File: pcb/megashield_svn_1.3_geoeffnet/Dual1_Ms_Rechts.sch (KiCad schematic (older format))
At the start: 7 parts, among them P18 Right

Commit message: Platine V1.3
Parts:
- renumbered BY1 to DBY1, BY2 to DBY2, BY3 to DBY3, BY4 to DBY4
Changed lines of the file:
@@
 LIBS:power
 LIBS:ardumower mega shield svn-cache
+LIBS:conn
 EELAYER 25 0
 EELAYER END
@@
 MotorRechtsB
 $Comp
-L +24V #PWR0137
+L +24V #PWR0139
 U 1 1 554BE90F
 P 4895 3310
-F 0 "#PWR0137" H 4895 3160 60  0001 C CNN
+F 0 "#PWR0139" H 4895 3160 60  0001 C CNN
 F 1 "+24V" H 4895 3450 60  0000 C CNN
 F 2 "" H 4895 3310 60  0000 C CNN
@@
 $EndComp
 $Comp
-L GND #PWR0138
+L GND #PWR0140
 U 1 1 554BE911
 P 4895 4445
-F 0 "#PWR0138" H 4895 4195 60  0001 C CNN
+F 0 "#PWR0140" H 4895 4195 60  0001 C CNN
 F 1 "GND" H 4895 4295 60  0000 C CNN
 F 2 "" H 4895 4445 60  0000 C CNN
@@
 $EndComp
 $Comp
-L DIODE BY3
+L DIODE DBY3
 U 1 1 554BE913
 P 4895 3580
-F 0 "BY3" H 4895 3680 40  0000 C CNN
+F 0 "DBY3" H 4895 3680 40  0000 C CNN
 F 1 "BY 500/1000" H 4895 3480 40  0000 C CNN
 F 2 "ACS712:Diode_liegend_BY500_1000_RM15" H 4895 3580 60  0001 C CNN
@@
 $EndComp
 $Comp
-L DIODE BY4
+L DIODE DBY4
 U 1 1 554BE915
 P 4895 4140
-F 0 "BY4" H 4895 4240 40  0000 C CNN
+F 0 "DBY4" H 4895 4240 40  0000 C CNN
 F 1 "BY 500/1000" H 4895 4040 40  0000 C CNN
 F 2 "ACS712:Diode_liegend_BY500_1000_RM15" H 4895 4140 60  0001 C CNN
@@
 Connection ~ 4895 3870
 $Comp
-L +24V #PWR0139
+L +24V #PWR0141
 U 1 1 554BE918
 P 3170 3310
-F 0 "#PWR0139" H 3170 3160 60  0001 C CNN
+F 0 "#PWR0141" H 3170 3160 60  0001 C CNN
 F 1 "+24V" H 3170 3450 60  0000 C CNN
 F 2 "" H 3170 3310 60  0000 C CNN
@@
 $EndComp
 $Comp
-L GND #PWR0140
+L GND #PWR0142
 U 1 1 554BE91A
 P 3170 4445
-F 0 "#PWR0140" H 3170 4195 60  0001 C CNN
+F 0 "#PWR0142" H 3170 4195 60  0001 C CNN
 F 1 "GND" H 3170 4295 60  0000 C CNN
 F 2 "" H 3170 4445 60  0000 C CNN
@@
 $EndComp
 $Comp
-L DIODE BY1
+L DIODE DBY1
 U 1 1 554BE91C
 P 3170 3580
-F 0 "BY1" H 3170 3680 40  0000 C CNN
+F 0 "DBY1" H 3170 3680 40  0000 C CNN
 F 1 "BY 500/1000" H 3170 3480 40  0000 C CNN
 F 2 "ACS712:Diode_liegend_BY500_1000_RM15" H 3170 3580 60  0001 C CNN
@@
 $EndComp
 $Comp
-L DIODE BY2
+L DIODE DBY2
 U 1 1 554BE91E
 P 3170 4140
-F 0 "BY2" H 3170 4240 40  0000 C CNN
+F 0 "DBY2" H 3170 4240 40  0000 C CNN
 F 1 "BY 500/1000" H 3170 4040 40  0000 C CNN
 F 2 "ACS712:Diode_liegend_BY500_1000_RM15" H 3170 4140 60  0001 C CNN

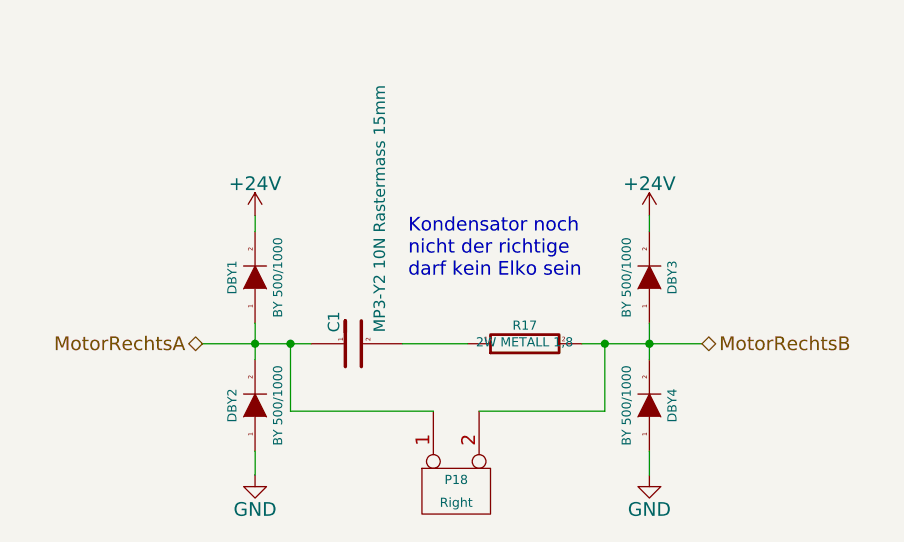
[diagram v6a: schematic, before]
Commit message: Platine V1.3
Einzelne Bauteile auf SMD angepasst
Belegung Anschlussstecker geändert +5V und GND
Anschlussstecker auf KK Stecker umgeändert
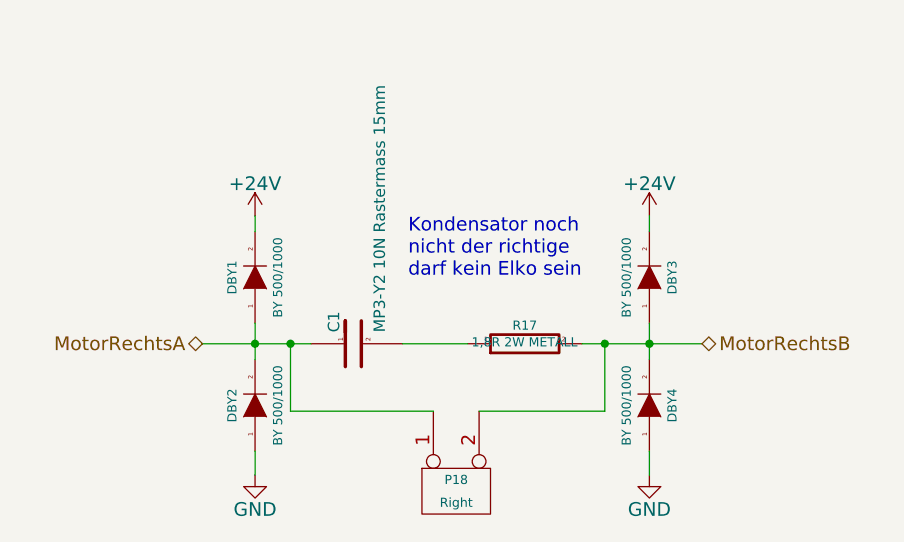
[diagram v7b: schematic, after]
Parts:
- DBY1, DBY2, DBY3, DBY4: footprint ACS712:Diode_liegend_BY500_1000_RM15 -> Diodes_ThroughHole:Diode_DO-201AD_Horizontal_RM15; Bauform (none) -> DO-201; Bestelllink (none) -> https://www.reichelt.de/BY-500-1000/3/index.html?&ACTION=3&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
- R17: value 2W METALL 1,8 -> 1,8R 2W METALL; footprint Resistors_ThroughHole:Resistor_Horizontal_RM20mm -> Resistors_SMD:R_2512
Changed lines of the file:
@@
 $Descr A4 11693 8268
 encoding utf-8
-Sheet 13 27
+Sheet 13 25
 Title "Ardumower Shield - Motortreiber 1 - Rechts"
 Date ""
@@
 MotorRechtsB
 $Comp
-L +24V #PWR0143
+L +24V #PWR0153
 U 1 1 554BE90F
 P 4895 3310
-F 0 "#PWR0143" H 4895 3160 60  0001 C CNN
+F 0 "#PWR0153" H 4895 3160 60  0001 C CNN
 F 1 "+24V" H 4895 3450 60  0000 C CNN
 F 2 "" H 4895 3310 60  0000 C CNN
@@
 $EndComp
 $Comp
-L GND #PWR0144
+L GND #PWR0154
 U 1 1 554BE911
 P 4895 4445
-F 0 "#PWR0144" H 4895 4195 60  0001 C CNN
+F 0 "#PWR0154" H 4895 4195 60  0001 C CNN
 F 1 "GND" H 4895 4295 60  0000 C CNN
 F 2 "" H 4895 4445 60  0000 C CNN
@@
 F 0 "DBY3" H 4895 3680 40  0000 C CNN
 F 1 "BY 500/1000" H 4895 3480 40  0000 C CNN
-F 2 "ACS712:Diode_liegend_BY500_1000_RM15" H 4895 3580 60  0001 C CNN
+F 2 "Diodes_ThroughHole:Diode_DO-201AD_Horizontal_RM15" H 4895 3580 60  0001 C CNN
 F 3 "https://www.reichelt.de/BY-500-1000/3/index.html?&ACTION=3&LA=446&ARTICLE=6337&artnr=BY+500%2F1000&SEARCH=BY+500%2F1000" H 4895 3580 60  0001 C CNN
-F 4 "R: BY 500/1000" H 4895 3580 60  0001 C CNN "Bestellnummer"
-F 5 "Fast-Recovery-Gleichr.-Diode, DO201, 1000V, 5A" H 4895 3580 60  0001 C CNN "Technische Daten"
+F 4 "Fast-Recovery-Gleichr.-Diode, DO201, 1000V, 5A" H 4895 3580 60  0001 C CNN "Technische Daten"
+F 5 "R: BY 500/1000" H 4895 3580 60  0001 C CNN "Bestellnummer"
+F 6 "DO-201" H 4895 3580 60  0001 C CNN "Bauform"
+F 7 "https://www.reichelt.de/BY-500-1000/3/index.html?&ACTION=3&LA=446&ARTICLE=6337&artnr=BY+500%2F1000&SEARCH=BY+500%2F1000" H 4895 3580 60  0001 C CNN "Bestelllink"
 	1    4895 3580
 	0    1    -1   0
@@
 F 0 "DBY4" H 4895 4240 40  0000 C CNN
 F 1 "BY 500/1000" H 4895 4040 40  0000 C CNN
-F 2 "ACS712:Diode_liegend_BY500_1000_RM15" H 4895 4140 60  0001 C CNN
+F 2 "Diodes_ThroughHole:Diode_DO-201AD_Horizontal_RM15" H 4895 4140 60  0001 C CNN
 F 3 "https://www.reichelt.de/BY-500-1000/3/index.html?&ACTION=3&LA=446&ARTICLE=6337&artnr=BY+500%2F1000&SEARCH=BY+500%2F1000" H 4895 4140 60  0001 C CNN
-F 4 "R: BY 500/1000" H 4895 4140 60  0001 C CNN "Bestellnummer"
-F 5 "Fast-Recovery-Gleichr.-Diode, DO201, 1000V, 5A" H 4895 4140 60  0001 C CNN "Technische Daten"
+F 4 "Fast-Recovery-Gleichr.-Diode, DO201, 1000V, 5A" H 4895 4140 60  0001 C CNN "Technische Daten"
+F 5 "R: BY 500/1000" H 4895 4140 60  0001 C CNN "Bestellnummer"
+F 6 "DO-201" H 4895 4140 60  0001 C CNN "Bauform"
+F 7 "https://www.reichelt.de/BY-500-1000/3/index.html?&ACTION=3&LA=446&ARTICLE=6337&artnr=BY+500%2F1000&SEARCH=BY+500%2F1000" H 4895 4140 60  0001 C CNN "Bestelllink"
 	1    4895 4140
 	0    1    -1   0
@@
 Connection ~ 4895 3870
 $Comp
-L +24V #PWR0145
+L +24V #PWR0155
 U 1 1 554BE918
 P 3170 3310
-F 0 "#PWR0145" H 3170 3160 60  0001 C CNN
+F 0 "#PWR0155" H 3170 3160 60  0001 C CNN
 F 1 "+24V" H 3170 3450 60  0000 C CNN
 F 2 "" H 3170 3310 60  0000 C CNN
@@
 $EndComp
 $Comp
-L GND #PWR0146
+L GND #PWR0156
 U 1 1 554BE91A
 P 3170 4445
-F 0 "#PWR0146" H 3170 4195 60  0001 C CNN
+F 0 "#PWR0156" H 3170 4195 60  0001 C CNN
 F 1 "GND" H 3170 4295 60  0000 C CNN
 F 2 "" H 3170 4445 60  0000 C CNN
@@
 F 0 "DBY1" H 3170 3680 40  0000 C CNN
 F 1 "BY 500/1000" H 3170 3480 40  0000 C CNN
-F 2 "ACS712:Diode_liegend_BY500_1000_RM15" H 3170 3580 60  0001 C CNN
+F 2 "Diodes_ThroughHole:Diode_DO-201AD_Horizontal_RM15" H 3170 3580 60  0001 C CNN
 F 3 "https://www.reichelt.de/BY-500-1000/3/index.html?&ACTION=3&LA=446&ARTICLE=6337&artnr=BY+500%2F1000&SEARCH=BY+500%2F1000" H 3170 3580 60  0001 C CNN
-F 4 "R: BY 500/1000" H 3170 3580 60  0001 C CNN "Bestellnummer"
-F 5 "Fast-Recovery-Gleichr.-Diode, DO201, 1000V, 5A" H 3170 3580 60  0001 C CNN "Technische Daten"
+F 4 "Fast-Recovery-Gleichr.-Diode, DO201, 1000V, 5A" H 3170 3580 60  0001 C CNN "Technische Daten"
+F 5 "R: BY 500/1000" H 3170 3580 60  0001 C CNN "Bestellnummer"
+F 6 "DO-201" H 3170 3580 60  0001 C CNN "Bauform"
+F 7 "https://www.reichelt.de/BY-500-1000/3/index.html?&ACTION=3&LA=446&ARTICLE=6337&artnr=BY+500%2F1000&SEARCH=BY+500%2F1000" H 3170 3580 60  0001 C CNN "Bestelllink"
 	1    3170 3580
 	0    -1   -1   0
@@
 F 0 "DBY2" H 3170 4240 40  0000 C CNN
 F 1 "BY 500/1000" H 3170 4040 40  0000 C CNN
-F 2 "ACS712:Diode_liegend_BY500_1000_RM15" H 3170 4140 60  0001 C CNN
+F 2 "Diodes_ThroughHole:Diode_DO-201AD_Horizontal_RM15" H 3170 4140 60  0001 C CNN
 F 3 "https://www.reichelt.de/BY-500-1000/3/index.html?&ACTION=3&LA=446&ARTICLE=6337&artnr=BY+500%2F1000&SEARCH=BY+500%2F1000" H 3170 4140 60  0001 C CNN
-F 4 "R: BY 500/1000" H 3170 4140 60  0001 C CNN "Bestellnummer"
-F 5 "Fast-Recovery-Gleichr.-Diode, DO201, 1000V, 5A" H 3170 4140 60  0001 C CNN "Technische Daten"
+F 4 "Fast-Recovery-Gleichr.-Diode, DO201, 1000V, 5A" H 3170 4140 60  0001 C CNN "Technische Daten"
+F 5 "R: BY 500/1000" H 3170 4140 60  0001 C CNN "Bestellnummer"
+F 6 "DO-201" H 3170 4140 60  0001 C CNN "Bauform"
+F 7 "https://www.reichelt.de/BY-500-1000/3/index.html?&ACTION=3&LA=446&ARTICLE=6337&artnr=BY+500%2F1000&SEARCH=BY+500%2F1000" H 3170 4140 60  0001 C CNN "Bestelllink"
 	1    3170 4140
 	0    -1   -1   0
@@
 P 4350 3870
 F 0 "R17" V 4430 3870 40  0000 C CNN
-F 1 "2W METALL 1,8" V 4357 3871 40  0000 C CNN
-F 2 "Resistors_ThroughHole:Resistor_Horizontal_RM20mm" V 4280 3870 30  0001 C CNN
+F 1 "1,8R 2W METALL" V 4357 3871 40  0000 C CNN
+F 2 "Resistors_SMD:R_2512" V 4280 3870 30  0001 C CNN
 F 3 "https://www.reichelt.de/2W-METALL-1-8/3/index.html?&ACTION=3&LA=446&ARTICLE=2309&artnr=2W+METALL+1%2C8&SEARCH=2W+METALL+1%2C8" H 4350 3870 30  0001 C CNN
 F 4 "R: 2W METALL 1,8" H 4350 3870 60  0001 C CNN "Bestellnummer"
